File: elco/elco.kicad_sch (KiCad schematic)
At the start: 18 parts, among them J2 Motor / Power, J3 IO, J4 Barrel_Jack_MountingPin, SW1 SW_DPDT_x2, U1 TPSM53602RDA

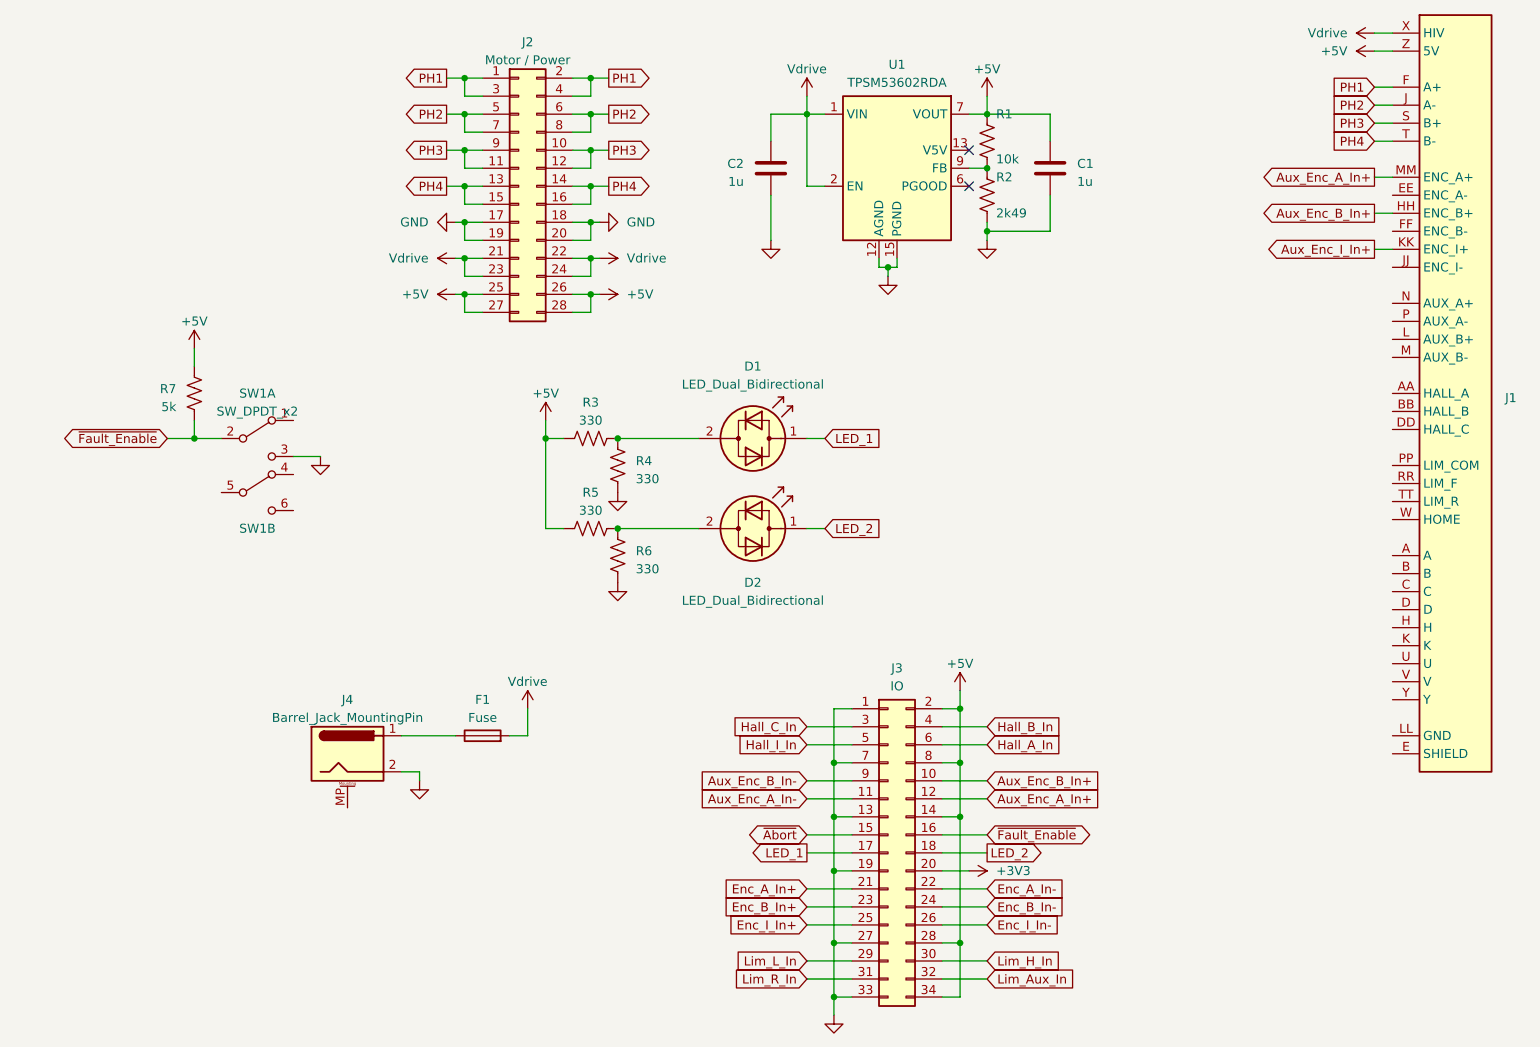
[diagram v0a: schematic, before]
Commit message: ELCO routing
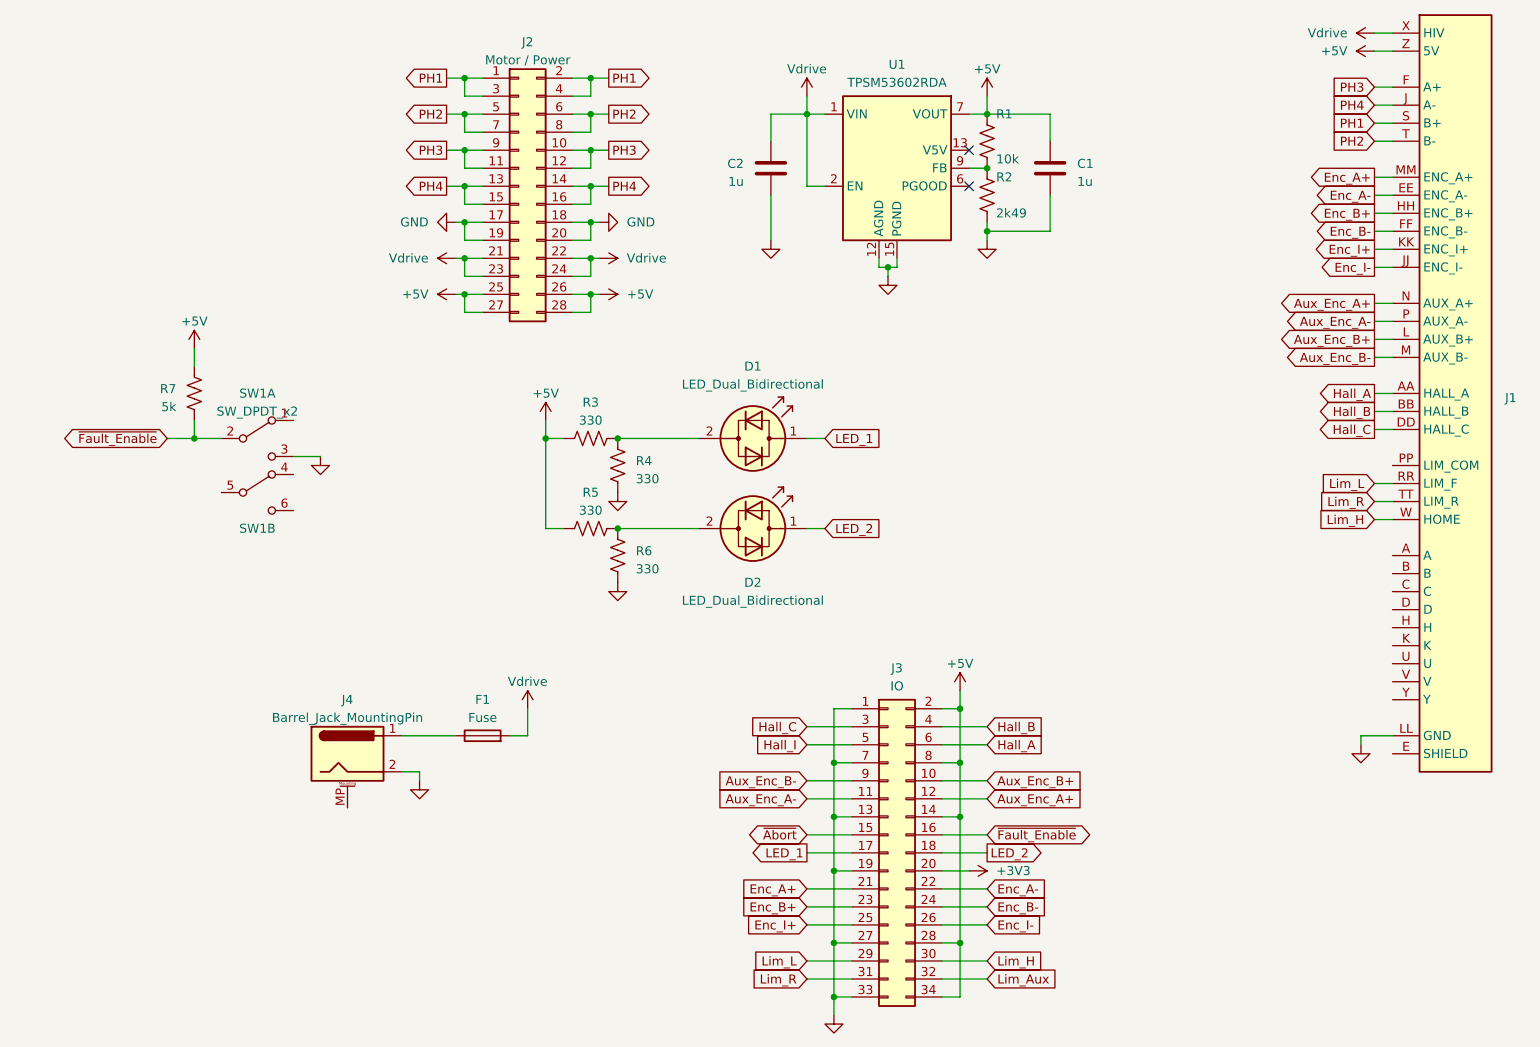
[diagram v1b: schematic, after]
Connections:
- net Aux_Enc_A_In- is gone; now on net Aux_Enc_A-: J3.11 (Pin_11)
- net Aux_Enc_B_In- is gone; now on net Aux_Enc_B-: J3.9 (Pin_9)
- net Enc_A_In+ is gone; now on net Enc_A+: J3.21 (Pin_21)
- net Enc_A_In- is gone; now on net Enc_A-: J3.22 (Pin_22)
- net Enc_B_In+ is gone; now on net Enc_B+: J3.23 (Pin_23)
- net Enc_B_In- is gone; now on net Enc_B-: J3.24 (Pin_24)
- net Enc_I_In+ is gone; now on net Enc_I+: J3.25 (Pin_25)
- net Enc_I_In- is gone; now on net Enc_I-: J3.26 (Pin_26)
- net Hall_A_In is gone; now on net Hall_A: J3.6 (Pin_6)
- net Hall_B_In is gone; now on net Hall_B: J3.4 (Pin_4)
- net Hall_C_In is gone; now on net Hall_C: J3.3 (Pin_3)
- net Lim_H_In is gone; now on net Lim_H: J3.30 (Pin_30)
- net Lim_L_In is gone; now on net Lim_L: J3.29 (Pin_29)
- net Lim_R_In is gone; now on net Lim_R: J3.31 (Pin_31)
- net GND: now also J1.LL (GND)
- net PH1: now also J1.S (B+); no longer J1.F (A+)
- net PH2: now also J1.T (B-); no longer J1.J (A-)
- net PH3: now also J1.F (A+); no longer J1.S (B+)
- net PH4: now also J1.J (A-); no longer J1.T (B-)
- net Hall_A: now reaches J1.AA (HALL_A)
- net Hall_B: now reaches J1.BB (HALL_B)
- net Hall_C: now reaches J1.DD (HALL_C)
- net Enc_A-: now reaches J1.EE (ENC_A-)
- net Enc_B-: now reaches J1.FF (ENC_B-)
- net Enc_I-: now reaches J1.JJ (ENC_I-)
- net Aux_Enc_B+: now reaches J1.L (AUX_B+)
- net Aux_Enc_B+: now also J3.10 (Pin_10)
- net Aux_Enc_B-: now reaches J1.M (AUX_B-)
- net Aux_Enc_A+: now reaches J1.N (AUX_A+)
- net Aux_Enc_A+: now also J3.12 (Pin_12)
- net Aux_Enc_A-: now reaches J1.P (AUX_A-)
- net Lim_L: now reaches J1.RR (LIM_F)
- net Lim_R: now reaches J1.TT (LIM_R)
- net Lim_H: now reaches J1.W (HOME)
- net Aux_Enc_A_In+ renamed Enc_A+
- net Enc_A+: no longer J3.12 (Pin_12)
- net Aux_Enc_B_In+ renamed Enc_B+
- net Enc_B+: no longer J3.10 (Pin_10)
- net Aux_Enc_I_In+ renamed Enc_I+
- net Hall_I_In renamed Hall_I
- net Lim_Aux_In renamed Lim_Aux

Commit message: Getting ready for fab
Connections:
- net PH3: now also J1.J (A-); no longer J1.F (A+)
- net PH4: now also J1.F (A+); no longer J1.J (A-)
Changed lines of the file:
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@@
     )
   )
-  (global_label "PH4" (shape input) (at 195.58 41.91 180) (fields_autoplaced)
+  (global_label "PH4" (shape input) (at 195.58 39.37 180) (fields_autoplaced)
     (effects (font (size 1.27 1.27)) (justify right))
-    (property "Intersheetrefs" "${INTERSHEET_REFS}" (at 188.8642 41.91 0)
+    (property "Intersheetrefs" "${INTERSHEET_REFS}" (at 188.8642 39.37 0)
       (effects (font (size 1.27 1.27)) (justify right) hide)
     )
@@
     )
   )
-  (global_label "PH3" (shape input) (at 195.58 39.37 180) (fields_autoplaced)
+  (global_label "PH3" (shape input) (at 195.58 41.91 180) (fields_autoplaced)
     (effects (font (size 1.27 1.27)) (justify right))
-    (property "Intersheetrefs" "${INTERSHEET_REFS}" (at 188.8642 39.37 0)
+    (property "Intersheetrefs" "${INTERSHEET_REFS}" (at 188.8642 41.91 0)
       (effects (font (size 1.27 1.27)) (justify right) hide)
     )
